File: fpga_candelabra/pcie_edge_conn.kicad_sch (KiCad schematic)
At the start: 35 parts, among them J3 Bus_PCI_Express_x16

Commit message: candelabra: add i-pex extension ports, remove FMC1
* update bank/mgt allocation
* add basic pcb floorplanning

Signed-off-by: Yichuan Gao <gaoyichuan000@gmail.com>
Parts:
- J3: footprint Connector_PCBEdge:BUS_PCIexpress_x16 -> CHIPSAlliance_Connector:PCIexpress_x16_FHFL
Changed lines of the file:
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@@
 			)
 		)
-		(property "Footprint" "Connector_PCBEdge:BUS_PCIexpress_x16"
+		(property "Footprint" "CHIPSAlliance_Connector:PCIexpress_x16_FHFL"
 			(at 62.23 87.63 0)
 			(effects

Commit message: fpga_candelabra: major revision
* Finish DDR4 & QSFP+ & PCIe layout
* Change FMC to LPC
* Add mikroBUS extension
* 12V input & PDN updates
* FPGA config updates

Signed-off-by: Yichuan Gao <gaoyichuan000@gmail.com>
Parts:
- J3: footprint CHIPSAlliance_Connector:PCIexpress_x16_FHFL -> CHIPSAlliance_Connector:PCI_Express_x16_Full_Height_280mm_Length
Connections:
- net PCIE_3V3_NC: now reaches J3.A10 (+3.3V), J3.A9 (+3.3V), J3.B8 (+3.3V)
- no-connect marks 19 -> 18

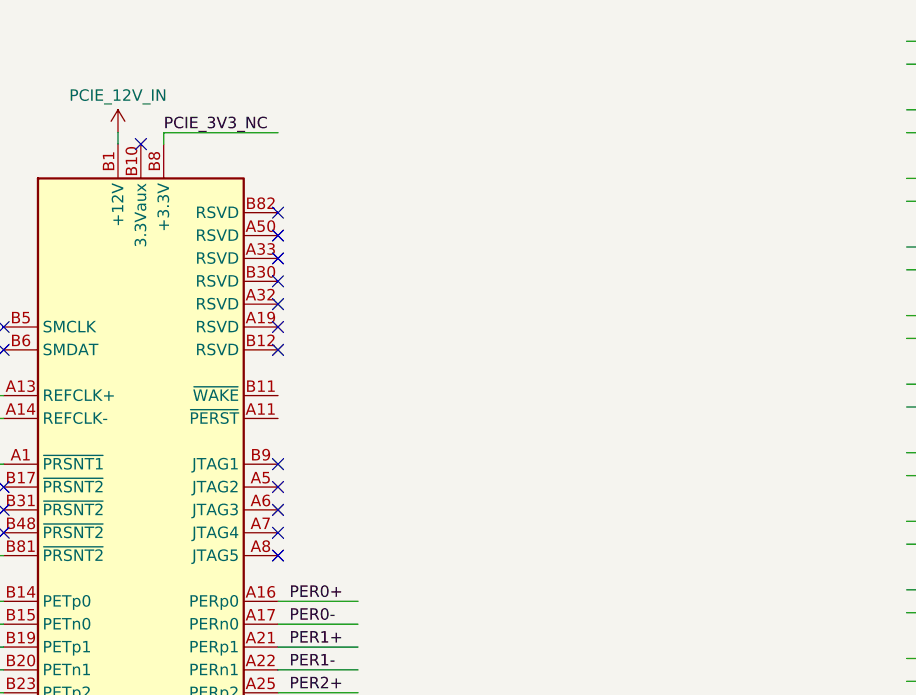
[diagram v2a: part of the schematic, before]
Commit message: fpga_candelabra: sch & layout v0.5, pass basic ERC & DRC
Signed-off-by: Yichuan Gao <gaoyichuan000@gmail.com>
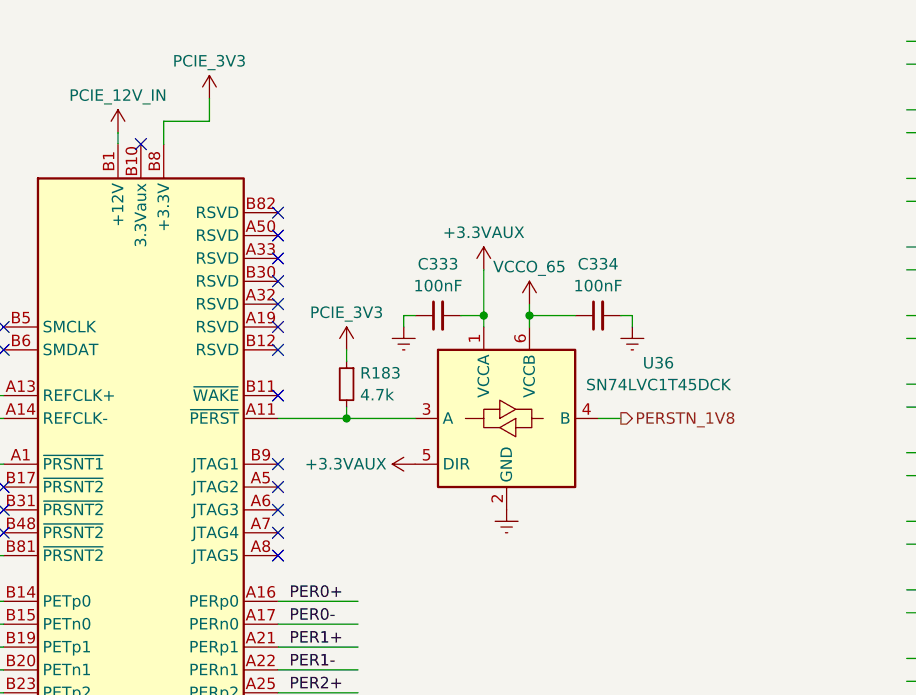
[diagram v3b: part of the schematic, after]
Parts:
- added C333, C334: 100nF, Capacitor_SMD:C_0402_1005Metric, symbol Device:C_Small
- added R183: 4.7k, Resistor_SMD:R_0402_1005Metric, symbol Device:R_Small
- added U36: SN74LVC1T45DCK, Package_TO_SOT_SMD:SOT-363_SC-70-6, symbol Logic_LevelTranslator:SN74LVC1T45DCK
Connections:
- net Earth: now also C333.1, C334.2, U36.2 (GND)
- net at J3.A11 (~{PERST}): now also R183.2, U36.3 (A)
- net PCIE_3V3_NC renamed PCIE_3V3
- net PCIE_3V3: now also R183.1
- new net +3.3VAUX: C333.2, U36.1 (VCCA), U36.5 (DIR)
- new net PERSTN_1V8: U36.4 (B)
- new net VCCO_65: C334.1, U36.6 (VCCB)
- no-connect marks 18 -> 19

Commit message: fpga_candelabra: add author & rev to schematics
Signed-off-by: Yichuan Gao <gaoyichuan000@gmail.com>
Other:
- company: (none) -> CHIPS Alliance
- title: (none) -> PCIe Edge Connector
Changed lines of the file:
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@@
 	(generator_version "8.0")
 	(paper "A4")
+	(title_block
+		(title "PCIe Edge Connector")
+		(date "2025-02-05")
+		(rev "0.2.0")
+		(company "CHIPS Alliance")
+		(comment 1 "Yichuan Gao")
+		(comment 2 "Yichuan Gao")
+	)
 	(junction
 		(at 105.41 60.96)

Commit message: fpga_candelabra: exclude pcie edge conn from BOM
Signed-off-by: Yichuan Gao <gaoyichuan000@gmail.com>
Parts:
- J3: now left out of the parts list
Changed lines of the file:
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@@
 		(unit 1)
 		(exclude_from_sim no)
-		(in_bom yes)
+		(in_bom no)
 		(on_board yes)
 		(dnp no)

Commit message: fpga_candelabra: update to kicad 9.0
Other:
- company: CHIPS Alliance -> Sipeed
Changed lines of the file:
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@@
 (kicad_sch
-	(version 20231120)
+	(version 20250114)
 	(generator "eeschema")
-	(generator_version "8.0")
+	(generator_version "9.0")
 	(paper "A4")
 	(title_block
@@
 		(date "2025-02-05")
 		(rev "0.2.0")
-		(company "CHIPS Alliance")
-		(comment 1 "Yichuan Gao")
-		(comment 2 "Yichuan Gao")
+		(company "Sipeed")
+		(comment 1 "Sipeed")
+		(comment 2 "Sipeed")
 	)
 	(junction
